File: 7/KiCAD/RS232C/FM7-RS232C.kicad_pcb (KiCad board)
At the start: 2 copper layers, 123.2 x 77.5 mm, 41 parts, among them CN2 DB9_Male, M10 74LS04, M11 8251A, M12 74LS27, M13 74LS11, M2 74LS38, M3 75188, M4 75189, M5 74LS00, M6 74LS32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

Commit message: Updating PCB
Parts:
- added JP10: Jumper_NC_Small, Connector_PinHeader_2.54mm:PinHeader_1x02_P2.54mm_Vertical, F.Cu at (129.8, 63.0)
- added JP11: Jumper_NC_Small, Connector_PinHeader_2.54mm:PinHeader_1x02_P2.54mm_Vertical, F.Cu at (132.6, 65.5)
- JP1: renamed from J1; value (none) -> Jumper_NO_Small
- JP2: renamed from J2; value (none) -> Jumper_NO_Small
- JP3: renamed from J3; value (none) -> Jumper_NO_Small
- JP4: renamed from J4; value (none) -> Jumper_NO_Small
- JP5: renamed from J5; value (none) -> Jumper_NC_Small
- moved C2 3.05 mm to (137.7, 64.1)
- moved R3 3.05 mm to (147.8, 68.6)
- moved R5 2.41 mm to (160.5, 68.6)
- renumbered A1 to CN_A1, B1 to CN_B1
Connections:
- net Net-(CN_A1-Pad1) renamed /EAB0
- net Net-(CN_A1-Pad3) renamed /EAB4
- net Net-(CN_B1-Pad2) renamed /EAB3
- net Net-(CN_B1-Pad9) renamed /EE
- CN_A1 pad 2: Net-(CN_A1-Pad2) -> /EAB2
- CN_A1 pad 4: Net-(CN_A1-Pad4) -> /EAB6
- CN_B1 pad 1: Net-(CN_B1-Pad1) -> /EAB1
- CN_B1 pad 3: Net-(CN_B1-Pad3) -> /EAB5
- CN_B1 pad 4: Net-(CN_B1-Pad4) -> /EAB7
- M10 pad 6: /~ERQ -> /~ERW
- M12 pad 10: Net-(M12-Pad10) -> /~EIOS
- M12 pad 12: /AB34 -> /AB347
- M12 pad 13: GND -> /EAB7
- M12 pad 3: Net-(CN_B1-Pad4) -> /EAB6
- M12 pad 4: Net-(CN_A1-Pad4) -> /EAB6
- M12 pad 5: Net-(CN_B1-Pad3) -> /EAB5or1
- M12 pad 6: /AB567 -> /AB56
- M12 pad 9: /~EIOS -> Net-(M12-Pad9)
- M13 pad 1: Net-(CN_A1-Pad2) -> /EAB2
- M13 pad 11: +5V -> /~ERW
- M13 pad 13: +5V -> /EAB1or5
- M13 pad 2: Net-(CN_B1-Pad1) -> /EAB2
- M13 pad 3: /AB34 -> /AB56
- M13 pad 4: Net-(M13-Pad12) -> /AB347
- M13 pad 5: /AB567 -> Net-(M13-Pad12)
- M5 pad 1: (no net) -> Net-(M5-Pad1)
- M5 pad 12: /~ERQ -> /~ERW
- M5 pad 2: (no net) -> Net-(M5-Pad1)
- M5 pad 3: (no net) -> Net-(M5-Pad3)
- M6 pad 1: (no net) -> /EAB5
- M6 pad 2: (no net) -> /EAB6
- M6 pad 3: (no net) -> Net-(M5-Pad1)
- M6 pad 8: Net-(M12-Pad11) -> Net-(M12-Pad9)
- M6 pad 9: Net-(CN_A1-Pad2) -> /EAB2
- M7 pad 1: /~ERQ -> Net-(M5-Pad3)
- M7 pad 3: /AB567 -> /AB347
- M7 pad 4: /AB34 -> /EAB1
- M7 pad 5: Net-(CN_B1-Pad1) -> /EAB1
- M7 pad 6: Net-(M12-Pad10) -> Net-(M12-Pad11)
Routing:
- net /~ERQ: track 158.9 -> 0.00 mm, vias 1 -> 0
- net /EAB1: track 0.00 -> 85.2 mm
- net /EAB2: track 0.00 -> 83.4 mm, vias 0 -> 1
- net Net-(CN_A1-Pad2): track 73.5 -> 0.00 mm, vias 1 -> 0
- net /AB567: track 69.0 -> 0.00 mm, vias 1 -> 0
- net Net-(CN_B1-Pad1): track 63.6 -> 0.00 mm
- net /EAB5: track 0.00 -> 56.1 mm, vias 0 -> 1
- net /AB347: track 0.00 -> 42.6 mm, vias 0 -> 1
- net /AB56: track 0.00 -> 39.8 mm, vias 0 -> 1
- net /EAB7: track 0.00 -> 38.4 mm, vias 0 -> 1
- net /AB34: track 35.8 -> 0.00 mm
- net Net-(M12-Pad10): track 33.2 -> 0.00 mm
- net Net-(CN_B1-Pad4): track 32.0 -> 0.00 mm
- net /EAB1or5: track 0.00 -> 31.8 mm
- net Net-(CN_B1-Pad3): track 27.7 -> 0.00 mm
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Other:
- board text added: "Ver.20211115"
- board text removed: "Ver.20190107"

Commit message: Updated PCB
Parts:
- moved R4 0.38 mm to (158.5, 64.8)
- moved R5 0.38 mm to (160.9, 68.6)
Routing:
- net /~ERW: track 0.00 -> 205.9 mm, vias 0 -> 6
- net /EAB5: track 56.1 -> 147.6 mm, vias 1 -> 4
- net /EAB1: track 85.2 -> 154.8 mm, vias 0 -> 2
- net /EAB5or1: track 0.00 -> 68.3 mm, vias 0 -> 2
- net /EAB1or5: track 31.8 -> 94.9 mm, vias 0 -> 1
- net /EAB6: track 27.1 -> 65.7 mm, vias 0 -> 2
- net /EAB7: track 38.4 -> 65.3 mm, vias 1 -> 3
- net Net-(M11-Pad11): track 83.1 -> 77.5 mm
- net -12V: track 204.4 -> 201.1 mm
- net +5V: track 602.6 -> 600.2 mm
- net GND: track 623.8 -> 625.7 mm
- net /EE: track 180.1 -> 178.4 mm
- net /QORE: track 28.3 -> 29.9 mm
- net Net-(M4-Pad2): track 43.3 -> 44.9 mm
- net Net-(M11-Pad15): track 79.2 -> 77.8 mm
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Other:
- board text added: "COM0"
- board text added: "COM1"

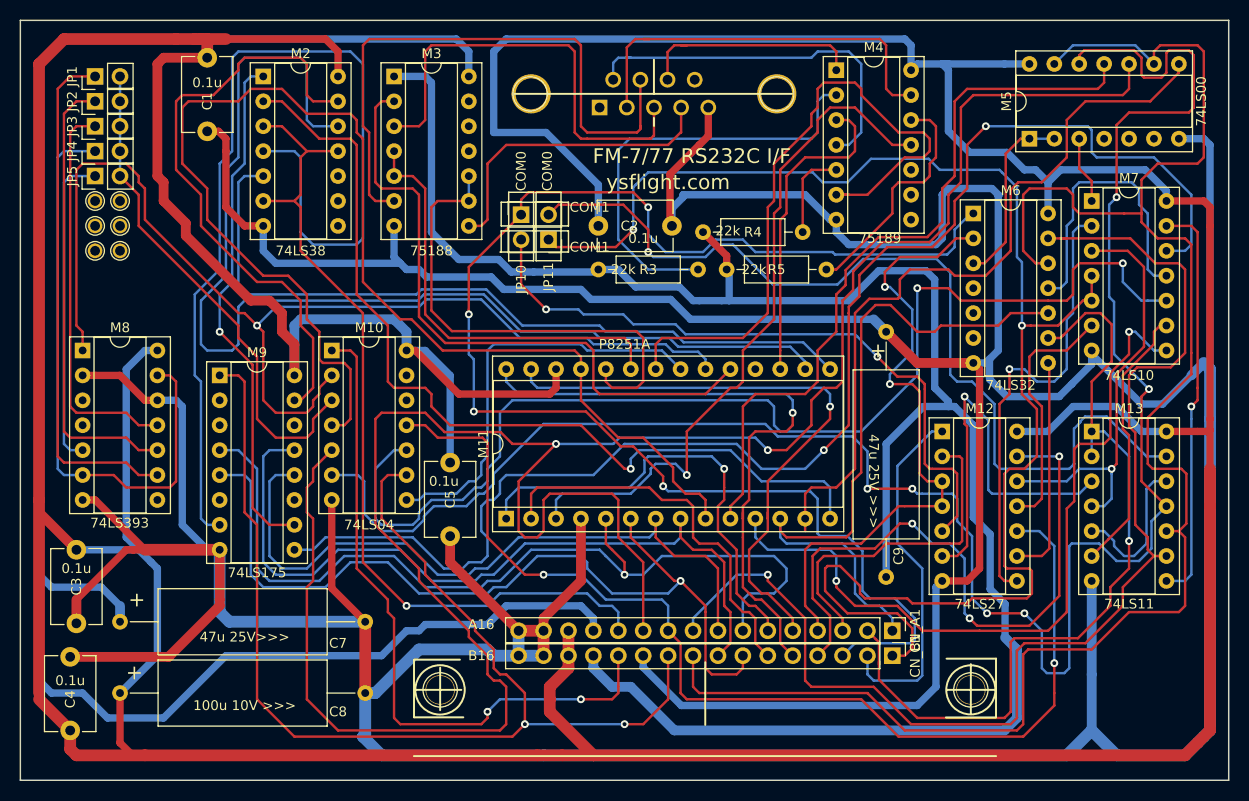
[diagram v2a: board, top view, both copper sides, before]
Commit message: Added +5V, GND pads.  Unofficially added JP6.  38400bps was already unofficial.
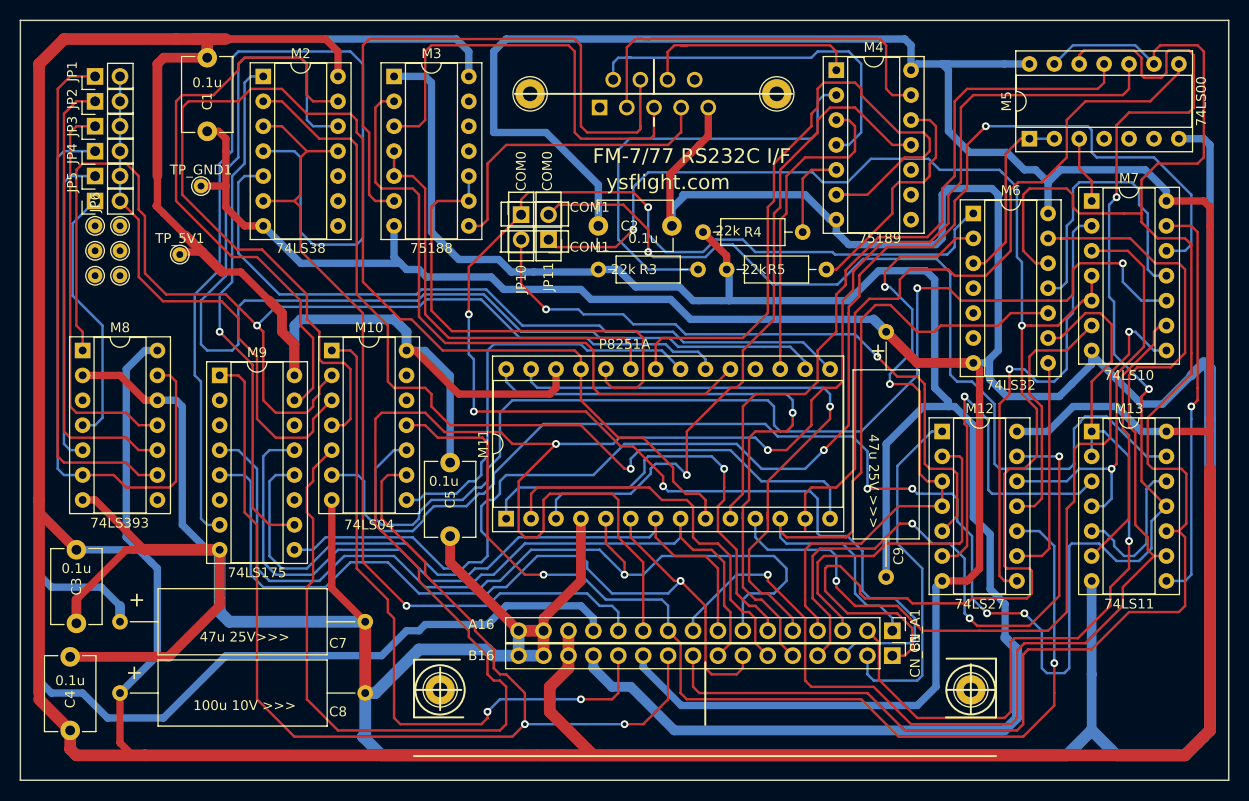
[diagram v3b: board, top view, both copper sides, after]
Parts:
- added JP6: Jumper_NO_Small, Connector_PinHeader_2.54mm:PinHeader_1x02_P2.54mm_Vertical, F.Cu at (86.4, 61.6)
- added TP_5V1: TestPoint, TestPoint:TestPoint_THTPad_D1.5mm_Drill0.7mm, F.Cu at (95.0, 67.1)
- added TP_GND1: TestPoint, TestPoint:TestPoint_THTPad_D1.5mm_Drill0.7mm, F.Cu at (97.2, 60.1)
- moved ? 7.62 mm to (86.4, 69.2)
- moved ? 7.62 mm to (88.9, 69.2)
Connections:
- net Net-(JP1-Pad1) renamed /2400bps
- net Net-(JP2-Pad1) renamed /4800bps
- net Net-(JP3-Pad1) renamed /9600bps
- net Net-(JP4-Pad1) renamed /19200bps
- net Net-(JP5-Pad1) renamed /38400bps
- M8 pad 4: Net-(M8-Pad4) -> /76800bps
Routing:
- net /76800bps: track 0.00 -> 26.7 mm
- net Net-(JP1-Pad2): track 51.4 -> 54.9 mm
- net Net-(M10-Pad2): track 114.5 -> 117.7 mm
- net +5V: track 600.2 -> 602.7 mm
- net Net-(M11-Pad15): track 77.8 -> 75.7 mm
- net GND: track 625.7 -> 626.7 mm

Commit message: Optimizing PCB
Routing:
- net /~ERW: track 205.9 -> 241.7 mm, vias 6 -> 4
- net /AB56: track 40.1 -> 46.4 mm
- net /EAB1: track 154.8 -> 159.9 mm, vias 2 -> 1
- net /EAB3: track 36.4 -> 31.6 mm
- net /AB347: track 43.5 -> 47.3 mm, vias 1 -> 0
- net Net-(M12-Pad8): track 46.8 -> 49.6 mm
- net /EQ: track 124.6 -> 127.2 mm
- net /EAB2: track 83.1 -> 85.4 mm
- net -12V: track 201.1 -> 203.2 mm
- net /EAB6: track 65.7 -> 67.6 mm
- net Net-(M11-Pad11): track 77.5 -> 76.0 mm, vias 2 -> 1
- net /EE: track 178.4 -> 179.7 mm
- net /EAB4: track 34.2 -> 35.2 mm
- net /EAB0: track 73.0 -> 73.7 mm
- net /EAB7: track 65.3 -> 66.1 mm, vias 3 -> 2
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
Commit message: Optimizing PCB
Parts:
- moved C2 0.76 mm to (137.7, 63.4)
- moved R3 0.76 mm to (147.1, 68.6)
- moved JP11 0.13 mm to (132.5, 65.5)
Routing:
- net /~ERW: track 241.7 -> 207.0 mm, vias 4 -> 3
- net Net-(M4-Pad2): track 44.9 -> 32.5 mm, vias 0 -> 1
- net /EAB7: track 66.1 -> 55.2 mm, vias 2 -> 1
- net Net-(M13-Pad8): track 41.4 -> 48.1 mm, vias 1 -> 0
- net /EAB1: track 159.9 -> 166.4 mm, vias 1 -> 0
- net Net-(M12-Pad8): track 49.6 -> 43.2 mm
- net /EAB2: track 85.4 -> 79.1 mm, vias 1 -> 0
- net /AB347: track 47.3 -> 53.1 mm
- net Net-(M13-Pad12): track 15.4 -> 9.72 mm
- net /EQ: track 127.2 -> 123.8 mm
- net /~WFD02: track 143.1 -> 140.0 mm
- net /EAB4: track 35.2 -> 38.3 mm
- net Net-(M10-Pad8): track 42.6 -> 45.1 mm
- net /EAB6: track 67.6 -> 69.9 mm
- net Net-(M10-Pad10): track 118.9 -> 117.1 mm, vias 2 -> 1
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
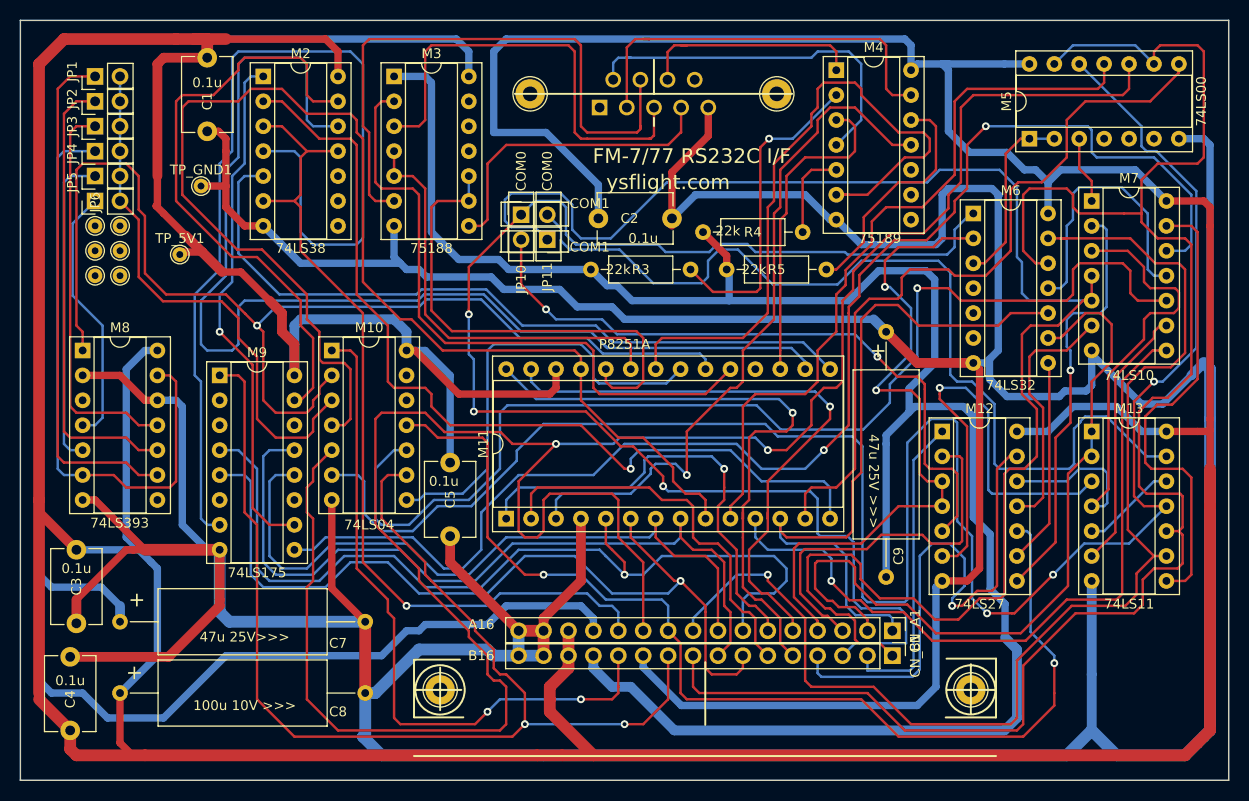
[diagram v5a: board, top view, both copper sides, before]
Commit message: Corrected hole drill size of FM-7 RS 232C card.
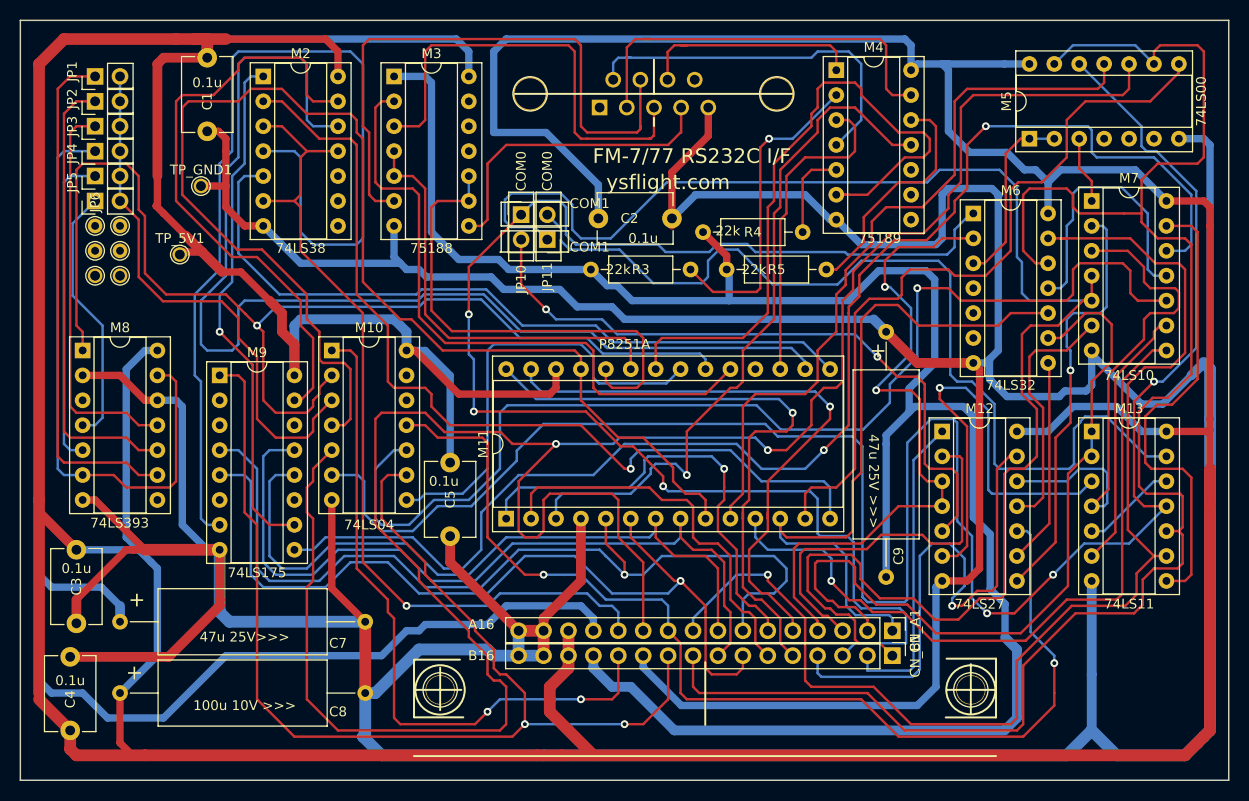
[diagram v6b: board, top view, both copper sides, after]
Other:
- board text added: "Ver.20220408"
- board text removed: "Ver.20211115"

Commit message: Updated FM-7 RS232C schematic and PCB.  It supports COM1 by jumper pins.
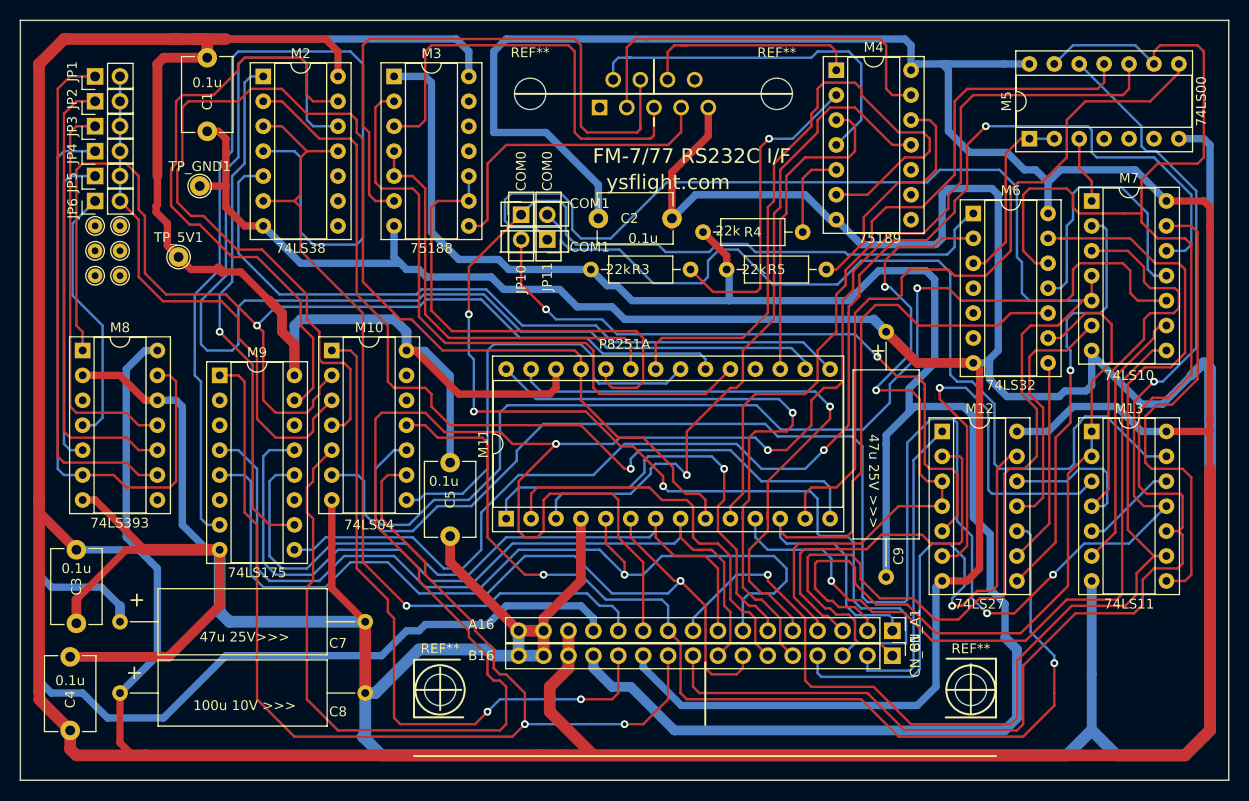
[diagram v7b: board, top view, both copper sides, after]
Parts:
- removed the ? at (155.9, 50.7)
- removed the ? at (130.7, 50.7)
- removed the ? at (175.6, 111.4)
- removed the ? at (121.5, 111.4)
- added REF**: 2.85mm, MountingHole:MountingHole_3.2mm_M3, F.Cu at (175.6, 111.4)
- added REF**: 2.85mm, MountingHole:MountingHole_3.2mm_M3, F.Cu at (121.5, 111.4)
- added REF**: 3.2mm, MountingHole:MountingHole_3.2mm_M3, F.Cu at (155.9, 50.7)
- added REF**: 3.2mm, MountingHole:MountingHole_3.2mm_M3, F.Cu at (130.7, 50.7)
- TP_5V1, TP_GND1: footprint TestPoint:TestPoint_THTPad_D1.5mm_Drill0.7mm -> TestPoint:TestPoint_THTPad_D2.0mm_Drill1.0mm
- moved TP_5V1 0.28 mm to (94.9, 67.3)
- moved TP_GND1 0.13 mm to (97.0, 60.1)
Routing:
- net Net-(M10-Pad4): track 129.9 -> 131.1 mm
- net Net-(M2-Pad13): track 61.3 -> 62.4 mm
- net +5V: track 601.3 -> 600.7 mm
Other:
- board text added: "Ver.20220412"
- board text removed: "Ver.20220408"
